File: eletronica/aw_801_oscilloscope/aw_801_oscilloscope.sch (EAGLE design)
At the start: 50 parts, among them IC1 ICL7660CPA, IC3 MEGA8-P, IC4 LM4558N, Q2 16Mhz, X2 USB

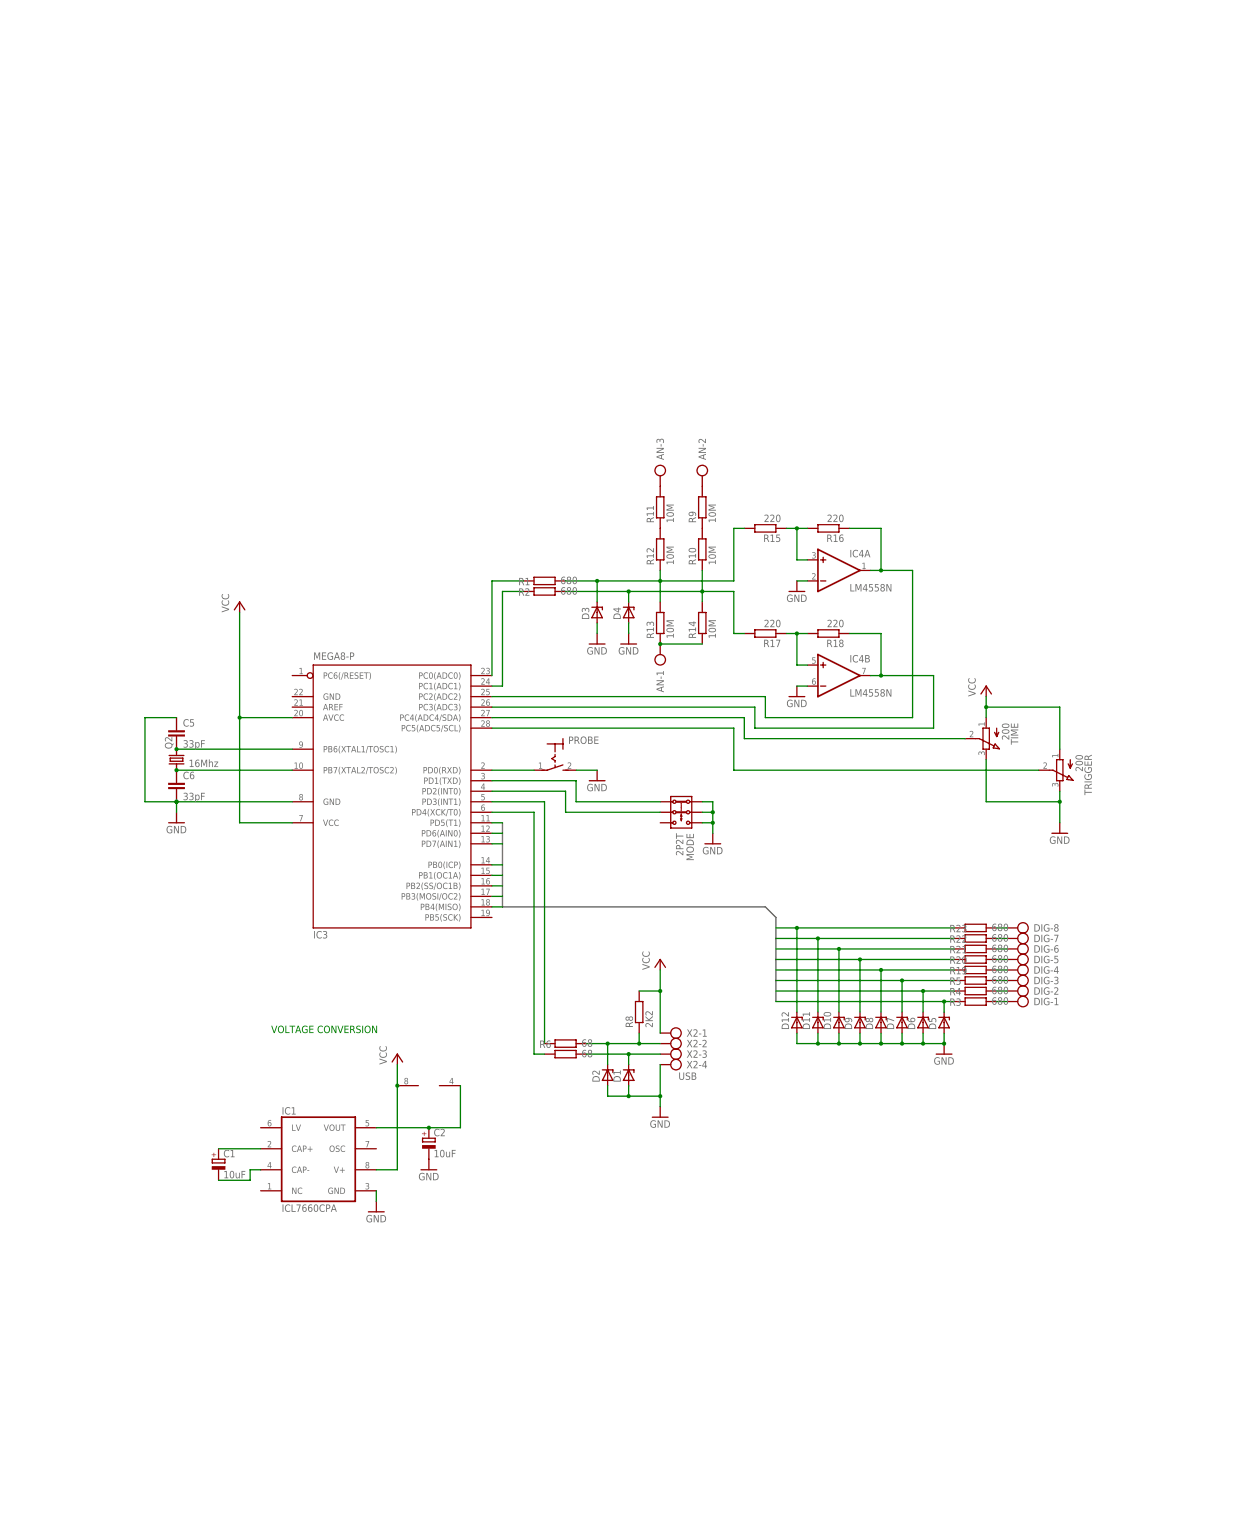
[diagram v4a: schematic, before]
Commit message: 
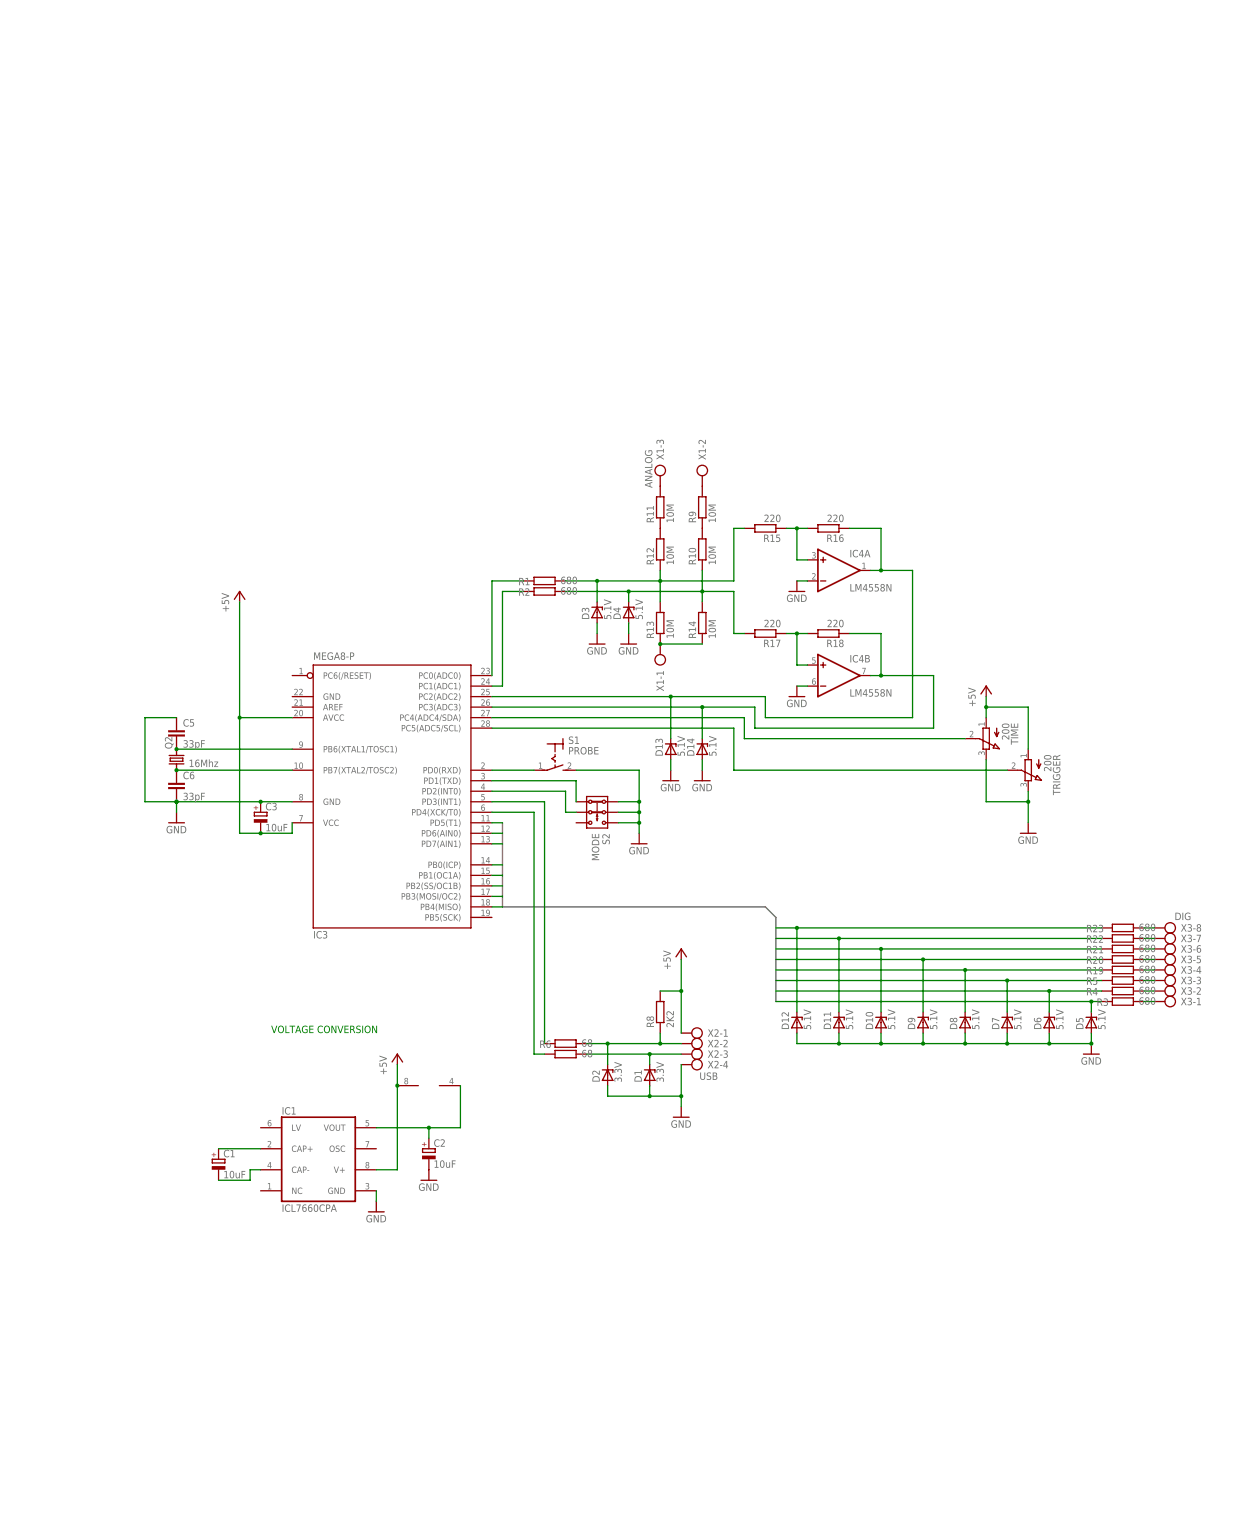
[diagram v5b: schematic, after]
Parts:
- removed DIG: (no value), con-ptr500:AK500/8
- removed MODE: 2P2T, switch:2P2T
- added C3: 10uF, rcl:CPOL-EUE2.5-6
- added D13, D14: 5.1V, diode:ZENER-DIODEDO35Z10
- added S2: MODE, switch:2P2T
- added X3: DIG, con-ptr500:AK500/8
- D1, D2: value (none) -> 3.3V
- D10, D11, D12, D3, D4, D5, D6, D7, D8, D9: value (none) -> 5.1V
- S1: value (none) -> PROBE
- X1: value (none) -> ANALOG
- renumbered AN to X1, PROBE to S1
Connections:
- removed net VCC: IC1.V+, IC3.AVCC, IC3.VCC@1, IC4P.V+, R8.2, TIME.A, TRIGGER.A, X2-1.KL
- new net +5V: C3.-, IC1.V+, IC3.AVCC, IC3.VCC@1, IC4P.V+, R8.2, TIME.A, TRIGGER.A, X2-1.KL
- net GND: now also C3.+, D13.A, D14.A, S2.1.1, S2.2.1, S2.3.1; no longer MODE.1.1, MODE.2.1, MODE.3.1
- net N$18: now also D13.C
- net N$20: now also D14.C
- net N$25: now also X3-8.KL; no longer DIG-8.KL
- net N$26: now also X3-7.KL; no longer DIG-7.KL
- net N$27: now also X3-6.KL; no longer DIG-6.KL
- net N$28: now also X3-5.KL; no longer DIG-5.KL
- net N$29: now also X3-4.KL; no longer DIG-4.KL
- net N$30: now also X3-3.KL; no longer DIG-3.KL
- net N$31: now also X3-2.KL; no longer DIG-2.KL
- net N$32: now also X3-1.KL; no longer DIG-1.KL
- net N$5: now also S2.1.2; no longer MODE.1.2
- net N$6: now also S2.2.2; no longer MODE.2.2
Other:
- moved on the sheet: C2, D1, D10, D11, D5, D6, D7, D8, D9, R19, R20, R21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

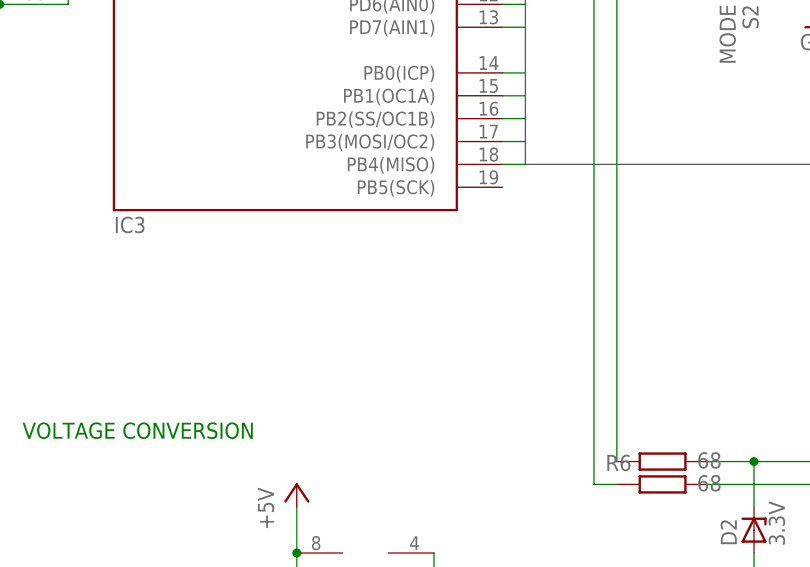
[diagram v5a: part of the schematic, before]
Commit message: 
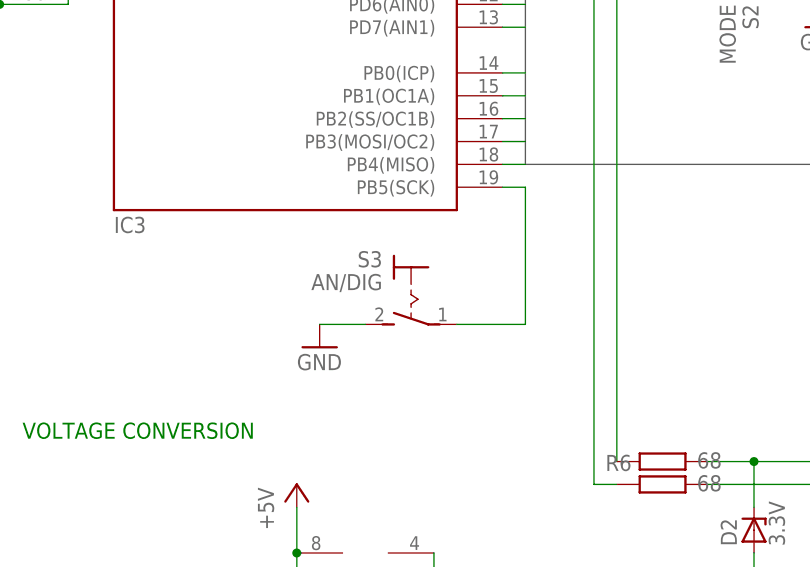
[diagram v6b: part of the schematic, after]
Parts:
- added S3: AN/DIG, switch:MS243
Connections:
- new net N$35: IC3.PB5(SCK), S3.P
- net GND: now also S3.S
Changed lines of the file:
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@@
 <part name="GND3" library="supply1" deviceset="GND" device=""/>
 <part name="GND13" library="supply1" deviceset="GND" device=""/>
+<part name="S3" library="switch" deviceset="MS243" device="" value="AN/DIG"/>
+<part name="GND14" library="supply1" deviceset="GND" device=""/>
 </parts>
 <sheets>
@@
 <instance part="GND3" gate="1" x="144.78" y="114.3"/>
 <instance part="GND13" gate="1" x="152.4" y="114.3"/>
+<instance part="S3" gate="1" x="91.44" y="68.58" rot="MR270"/>
+<instance part="GND14" gate="1" x="81.28" y="63.5"/>
 </instances>
 <busses>
@@
 <wire x1="152.4" y1="119.38" x2="152.4" y2="116.84" width="0.1524" layer="91"/>
 </segment>
+<segment>
+<pinref part="S3" gate="1" pin="S"/>
+<pinref part="GND14" gate="1" pin="GND"/>
+<wire x1="81.28" y1="66.04" x2="86.36" y2="66.04" width="0.1524" layer="91"/>
+</segment>
 </net>
 <net name="N$7" class="0">
@@
 </segment>
 </net>
+<net name="N$35" class="0">
+<segment>
+<pinref part="IC3" gate="G$1" pin="PB5(SCK)"/>
+<wire x1="101.6" y1="81.28" x2="104.14" y2="81.28" width="0.1524" layer="91"/>
+<wire x1="104.14" y1="81.28" x2="104.14" y2="66.04" width="0.1524" layer="91"/>
+<pinref part="S3" gate="1" pin="P"/>
+<wire x1="104.14" y1="66.04" x2="96.52" y2="66.04" width="0.1524" layer="91"/>
+</segment>
+</net>
